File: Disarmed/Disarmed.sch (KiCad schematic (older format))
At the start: 0 parts

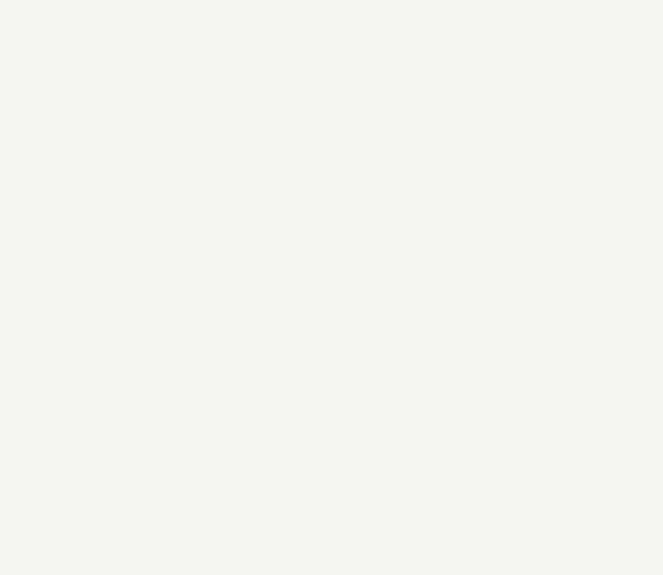
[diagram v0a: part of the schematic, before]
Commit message: Add LED Panel
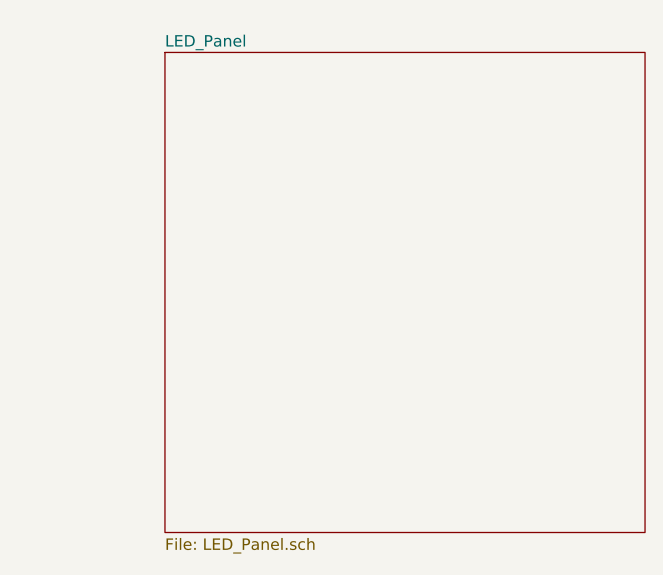
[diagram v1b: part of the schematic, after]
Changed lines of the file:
@@
 $Descr A4 11693 8268
 encoding utf-8
-Sheet 1 2
+Sheet 1 3
 Title ""
 Date ""
@@
 F1 "SSD_Panel.sch" 50
 $EndSheet
+$Sheet
+S 4000 950  2100 2100
+U 5FFDBE64
+F0 "LED_Panel" 50
+F1 "LED_Panel.sch" 50
+$EndSheet
 $EndSCHEMATC

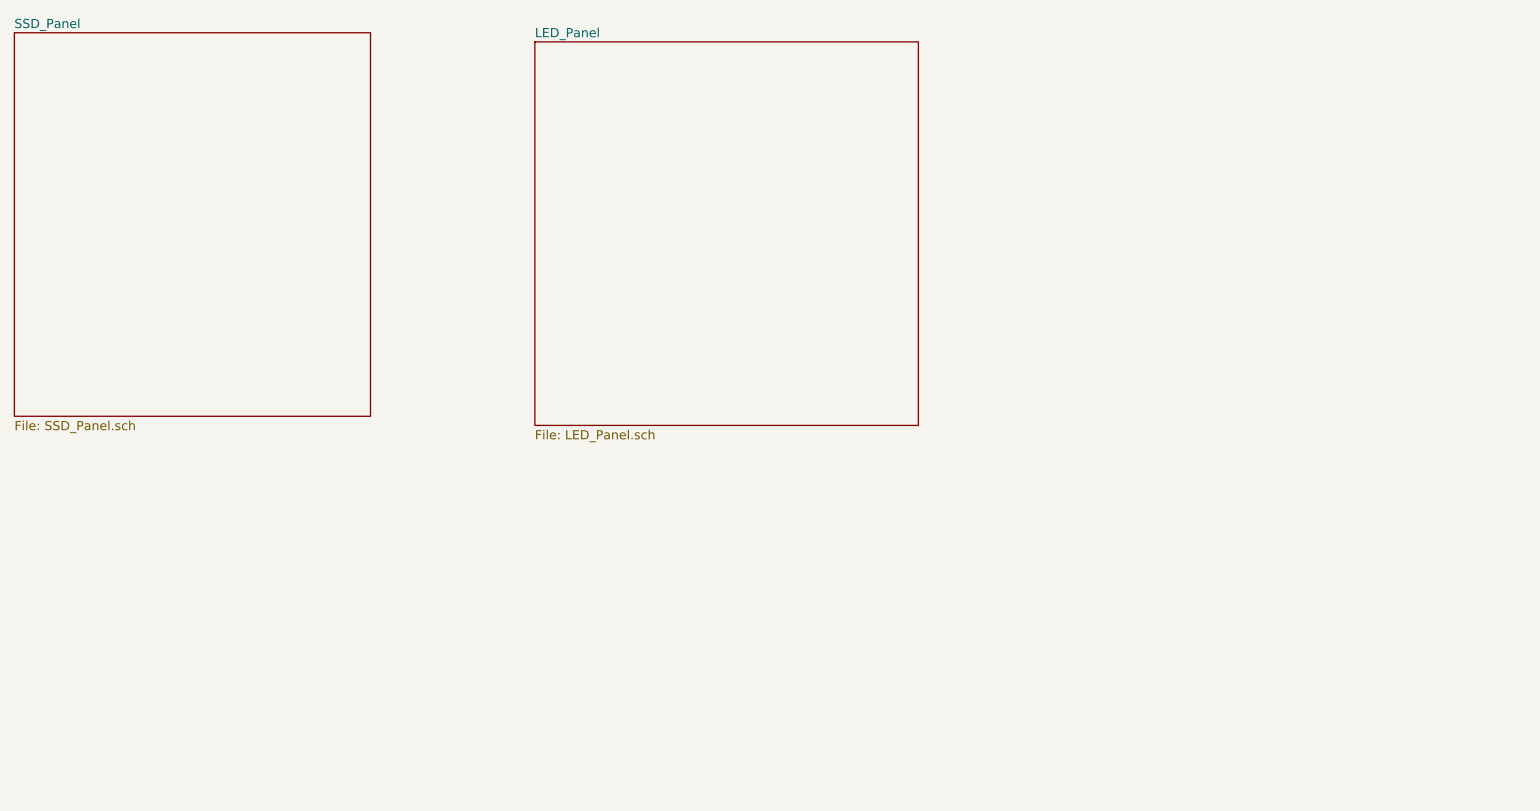
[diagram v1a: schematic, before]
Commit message: Board Update
Add Analog board v1, switch panel v1, remote ssd board v1
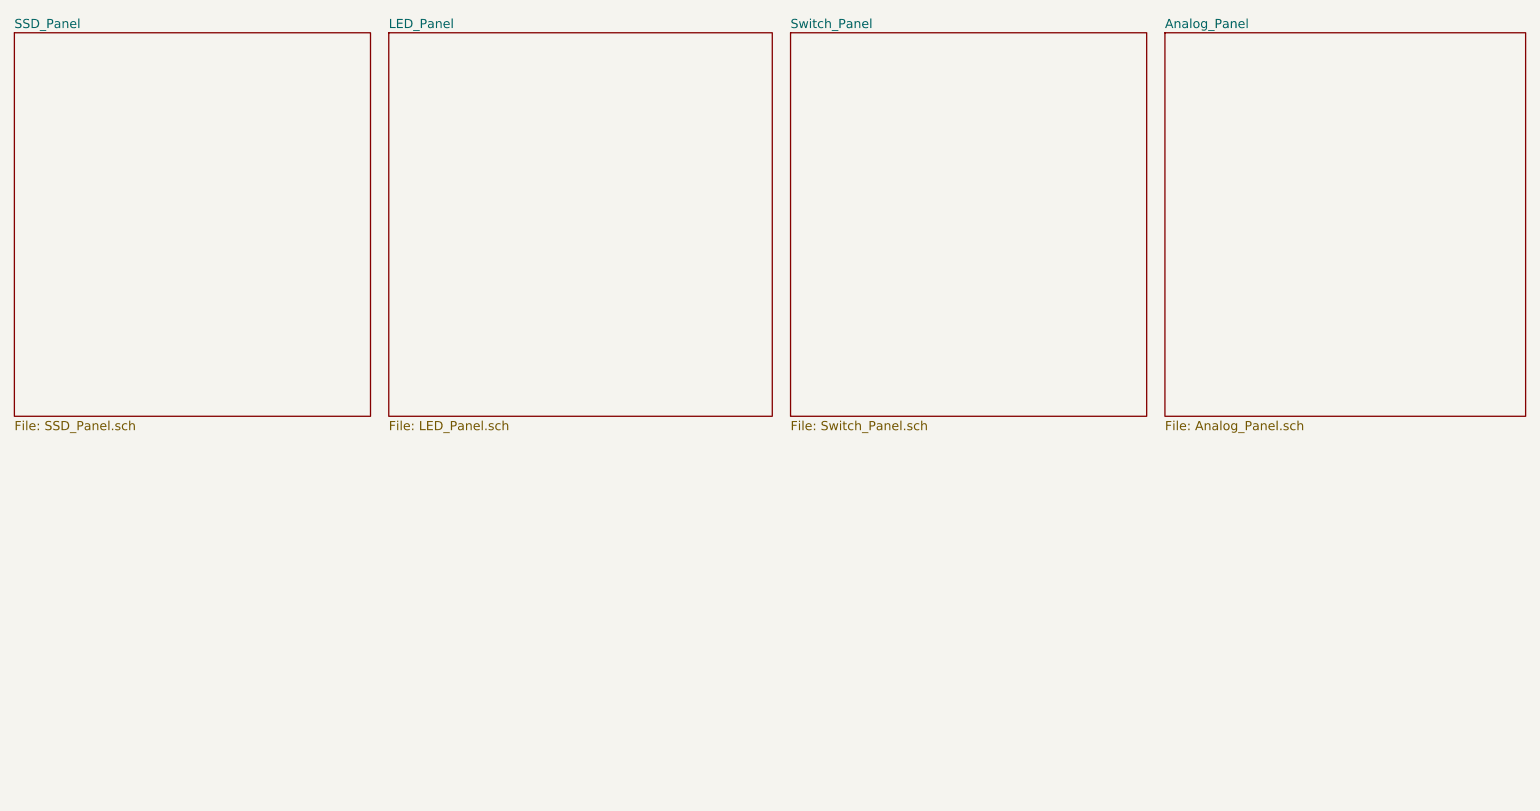
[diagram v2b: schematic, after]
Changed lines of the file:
@@
 $Descr A4 11693 8268
 encoding utf-8
-Sheet 1 3
+Sheet 1 5
 Title ""
 Date ""
@@
 $EndSheet
 $Sheet
-S 4000 950  2100 2100
+S 3200 900  2100 2100
 U 5FFDBE64
 F0 "LED_Panel" 50
 F1 "LED_Panel.sch" 50
 $EndSheet
+$Sheet
+S 5400 900  1950 2100
+U 60061CF4
+F0 "Switch_Panel" 50
+F1 "Switch_Panel.sch" 50
+$EndSheet
+$Sheet
+S 7450 900  1975 2100
+U 6008A670
+F0 "Analog_Panel" 50
+F1 "Analog_Panel.sch" 50
+$EndSheet
 $EndSCHEMATC

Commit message: Add new boards
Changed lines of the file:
@@
 $Descr A4 11693 8268
 encoding utf-8
-Sheet 1 5
+Sheet 1 6
 Title ""
 Date ""
@@
 F1 "Analog_Panel.sch" 50
 $EndSheet
+$Sheet
+S 5400 3375 1525 1600
+U 60463F34
+F0 "Switch_SSD_Row" 50
+F1 "Switch_SSD_Row.sch" 50
+$EndSheet
 $EndSCHEMATC
